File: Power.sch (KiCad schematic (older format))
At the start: 70 parts, among them J3 ESTOP, J4 PWR, J5 Conn_ARM_JTAG_SWD_10, J7 FAN, Q1 MMBT5401LT1G, Q2 PSMN4R8-100BSEJ, Q3 MMBT3904, Q4 Q_NMOS_GDS, Q5 Q_NMOS_GDS, Q6 Q_NMOS_GDS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

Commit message: add part numbers, minor tweaks
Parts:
- C44: footprint Capacitor_SMD:C_0402_1005Metric -> Capacitor_SMD:C_0603_1608Metric; D1PN 311-1039-1-ND -> (none); MFN Yageo -> (none); MPN CC0402KRX7R8BB472 -> (none)
- Q6: value Q_NMOS_GDS -> NTS4001NT1G; footprint Package_TO_SOT_SMD:SOT-416 -> Package_TO_SOT_SMD:SOT-323_SC-70; symbol Device:Q_NMOS_GDS -> Device:Q_NMOS_GSD
- R30: footprint Resistor_SMD:R_0402_1005Metric -> Resistor_SMD:R_0603_1608Metric; D1PN P432KHCT-ND -> (none); MFN Panasonic -> (none); MPN ERJ-3EKF4323V -> (none)
- R31: footprint Resistor_SMD:R_0402_1005Metric -> Resistor_SMD:R_0603_1608Metric
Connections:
- net +12V: now also Q6.3 (D); no longer Q6.2 (D)
- net at Q5.1 (G), R22.1: now also Q6.2 (S); no longer Q6.3 (S)
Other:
- moved on the sheet: C37, Q5, R21
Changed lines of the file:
@@
 Connection ~ 6650 3300
 Connection ~ 6925 1100
-Connection ~ 7000 5050
+Connection ~ 7000 5300
 Connection ~ 7000 5750
 Connection ~ 7000 6000
@@
 	6100 1450 6550 1450
 Wire Wire Line
+	6200 5300 6200 5700
+Wire Wire Line
+	6200 5300 7000 5300
+Wire Wire Line
+	6200 5900 6200 6000
+Wire Wire Line
+	6200 6000 7000 6000
+Wire Wire Line
 	6550 1100 6550 1150
 Wire Wire Line
@@
 	6550 1450 6550 1350
 Wire Wire Line
-	6600 5050 7000 5050
-Wire Wire Line
 	6650 3300 6450 3300
 Wire Wire Line
@@
 	7000 2100 6900 2100
 Wire Wire Line
-	7000 5050 7000 5000
-Wire Wire Line
-	7000 5350 7000 5050
-Wire Wire Line
-	7000 5750 7400 5750
+	7000 5300 7000 5250
+Wire Wire Line
+	7000 5350 7000 5300
+Wire Wire Line
+	7000 5750 7600 5750
 Wire Wire Line
 	7000 5800 7000 5750
 Wire Wire Line
-	7000 6000 7700 6000
+	7000 6000 7900 6000
 Wire Wire Line
 	7000 6050 7000 6000
@@
 	7700 1100 7500 1100
 Wire Wire Line
-	7700 6000 7700 5950
-Wire Wire Line
 	7800 1700 7950 1700
 Wire Wire Line
@@
 Wire Wire Line
 	7800 4250 7800 4050
+Wire Wire Line
+	7900 6000 7900 5950
 Wire Wire Line
 	7950 1900 7800 1900
@@
 Text GLabel 4850 900  2    50   Input ~ 0
 VOUT
-Text GLabel 7700 5350 1    50   Input ~ 0
+Text GLabel 7900 5350 1    50   Input ~ 0
 VOUT
 $Comp
@@
 L power:+12V #PWR0163
 U 1 1 5D69A634
-P 7000 5000
-F 0 "#PWR0163" H 7000 4850 50  0001 C CNN
-F 1 "+12V" H 7015 5173 50  0000 C CNN
-F 2 "" H 7000 5000 50  0001 C CNN
-F 3 "" H 7000 5000 50  0001 C CNN
-	1    7000 5000
+P 7000 5250
+F 0 "#PWR0163" H 7000 5100 50  0001 C CNN
+F 1 "+12V" H 7015 5423 50  0000 C CNN
+F 2 "" H 7000 5250 50  0001 C CNN
+F 3 "" H 7000 5250 50  0001 C CNN
+	1    7000 5250
 	1    0    0    -1
 $EndComp
@@
 F 3 "" H 5450 1450 50  0001 C CNN
 	1    5450 1450
-	-1   0    0    -1
-$EndComp
-$Comp
-L power:GND #PWR0145
-U 1 1 5E52C140
-P 6600 5250
-F 0 "#PWR0145" H 6600 5000 50  0001 C CNN
-F 1 "GND" H 6605 5077 50  0001 C CNN
-F 2 "" H 6600 5250 50  0001 C CNN
-F 3 "" H 6600 5250 50  0001 C CNN
-	1    6600 5250
 	-1   0    0    -1
 $EndComp
@@
 L Device:R_Small R21
 U 1 1 5D281236
-P 7700 5450
-F 0 "R21" H 7759 5496 50  0000 L CNN
-F 1 "10R" H 7759 5405 50  0000 L CNN
-F 2 "Package_TO_SOT_THT:TO-247-2_Vertical" H 7700 5450 50  0001 C CNN
-F 3 "~" H 7700 5450 50  0001 C CNN
-	1    7700 5450
+P 7900 5450
+F 0 "R21" H 7959 5496 50  0000 L CNN
+F 1 "10R" H 7959 5405 50  0000 L CNN
+F 2 "Package_TO_SOT_THT:TO-247-2_Vertical" H 7900 5450 50  0001 C CNN
+F 3 "~" H 7900 5450 50  0001 C CNN
+	1    7900 5450
 	1    0    0    -1
 $EndComp
@@
 F 0 "R30" H 10300 3750 50  0000 L CNN
 F 1 "437k" H 10300 3650 50  0000 L CNN
-F 2 "Resistor_SMD:R_0402_1005Metric" H 10200 3700 60  0001 C CNN
+F 2 "Resistor_SMD:R_0603_1608Metric" H 10200 3700 60  0001 C CNN
 F 3 "~" H 10200 3700 60  0001 C CNN
 F 4 "Digikey" H 10250 3800 50  0001 C CNN "D1N"
-F 5 "P432KHCT-ND" H 10250 3800 50  0001 C CNN "D1PN"
-F 6 "Panasonic" H 10250 3800 50  0001 C CNN "MFN"
-F 7 "ERJ-3EKF4323V" H 10250 3800 50  0001 C CNN "MPN"
+F 5 "" H 10250 3800 50  0001 C CNN "D1PN"
+F 6 "" H 10250 3800 50  0001 C CNN "MFN"
+F 7 "" H 10250 3800 50  0001 C CNN "MPN"
 F 8 "" H 10200 3700 60  0001 C CNN "Maximum Power"
 F 9 "432000" H 10200 3700 60  0001 C CNN "Resistance"
@@
 F 0 "R31" H 10300 4050 50  0000 L CNN
 F 1 "140k" H 10300 3950 50  0000 L CNN
-F 2 "Resistor_SMD:R_0402_1005Metric" H 10200 4000 60  0001 C CNN
+F 2 "Resistor_SMD:R_0603_1608Metric" H 10200 4000 60  0001 C CNN
 F 3 "~" H 10200 4000 60  0001 C CNN
 F 4 "Digikey" H 10250 4100 50  0001 C CNN "D1N"
@@
 $EndComp
 $Comp
+L Device:C_Small C37
+U 1 1 5D7A6A8D
+P 6200 5800
+F 0 "C37" H 6292 5846 50  0000 L CNN
+F 1 "100n" H 6292 5755 50  0000 L CNN
+F 2 "Capacitor_SMD:C_0603_1608Metric" H 6200 5800 50  0001 C CNN
+F 3 "~" H 6200 5800 50  0001 C CNN
+	1    6200 5800
+	1    0    0    -1
+$EndComp
+$Comp
 L Device:C_Small C40
 U 1 1 5D64F8F0
@@
 F 3 "~" H 6550 1250 50  0001 C CNN
 	1    6550 1250
-	1    0    0    -1
-$EndComp
-$Comp
-L Device:C_Small C37
-U 1 1 5D7A6A8D
-P 6600 5150
-F 0 "C37" H 6692 5196 50  0000 L CNN
-F 1 "100n" H 6692 5105 50  0000 L CNN
-F 2 "Capacitor_SMD:C_0603_1608Metric" H 6600 5150 50  0001 C CNN
-F 3 "~" H 6600 5150 50  0001 C CNN
-	1    6600 5150
 	1    0    0    -1
 $EndComp
@@
 F 0 "C44" H 9400 3850 50  0000 L CNN
 F 1 "4n7" H 9400 3950 50  0000 L CNN
-F 2 "Capacitor_SMD:C_0402_1005Metric" H 9300 3950 60  0001 C CNN
+F 2 "Capacitor_SMD:C_0603_1608Metric" H 9300 3950 60  0001 C CNN
 F 3 "~" H 9300 3950 60  0001 C CNN
 F 4 "4n7" H 9300 3950 60  0001 C CNN "Capacitance"
 F 5 "Digikey" H 9400 4000 50  0001 C CNN "D1N"
-F 6 "311-1039-1-ND" H 9400 4000 50  0001 C CNN "D1PN"
-F 7 "Yageo" H 9400 4000 50  0001 C CNN "MFN"
-F 8 "CC0402KRX7R8BB472" H 9400 4000 50  0001 C CNN "MPN"
+F 6 "" H 9400 4000 50  0001 C CNN "D1PN"
+F 7 "" H 9400 4000 50  0001 C CNN "MFN"
+F 8 "" H 9400 4000 50  0001 C CNN "MPN"
 F 9 "25V" H 9400 4050 50  0000 L CNN "Maximum Voltage"
 F 10 "10%" H 9300 3950 60  0001 C CNN "Tolerance"
@@
 $EndComp
 $Comp
-L Device:Q_NMOS_GDS Q6
+L Device:Q_NMOS_GSD Q6
 U 1 1 5D69534E
 P 6900 5550
-F 0 "Q6" H 6950 5750 50  0000 C CNN
-F 1 "Q_NMOS_GDS" V 7152 5550 50  0001 C CNN
-F 2 "Package_TO_SOT_SMD:SOT-416" H 7100 5650 50  0001 C CNN
+F 0 "Q6" H 7150 5700 50  0000 C CNN
+F 1 "NTS4001NT1G" H 7350 5600 50  0000 C CNN
+F 2 "Package_TO_SOT_SMD:SOT-323_SC-70" H 7100 5650 50  0001 C CNN
 F 3 "~" H 6900 5550 50  0001 C CNN
 	1    6900 5550
@@
 L Device:Q_NMOS_GDS Q5
 U 1 1 5D27FC20
-P 7600 5750
-F 0 "Q5" H 7550 5900 50  0000 C CNN
-F 1 "Q_NMOS_GDS" V 7948 5600 50  0001 C CNN
-F 2 "Package_TO_SOT_SMD:TO-263-2" H 7800 5850 50  0001 C CNN
-F 3 "~" H 7600 5750 50  0001 C CNN
-	1    7600 5750
-	1    0    0    -1
-$EndComp
+P 7800 5750
+F 0 "Q5" H 7750 5900 50  0000 C CNN
+F 1 "Q_NMOS_GDS" V 8148 5600 50  0001 C CNN
+F 2 "Package_TO_SOT_SMD:TO-263-2" H 8000 5850 50  0001 C CNN
+F 3 "~" H 7800 5750 50  0001 C CNN
+	1    7800 5750
+	1    0    0    -1
+$EndComp

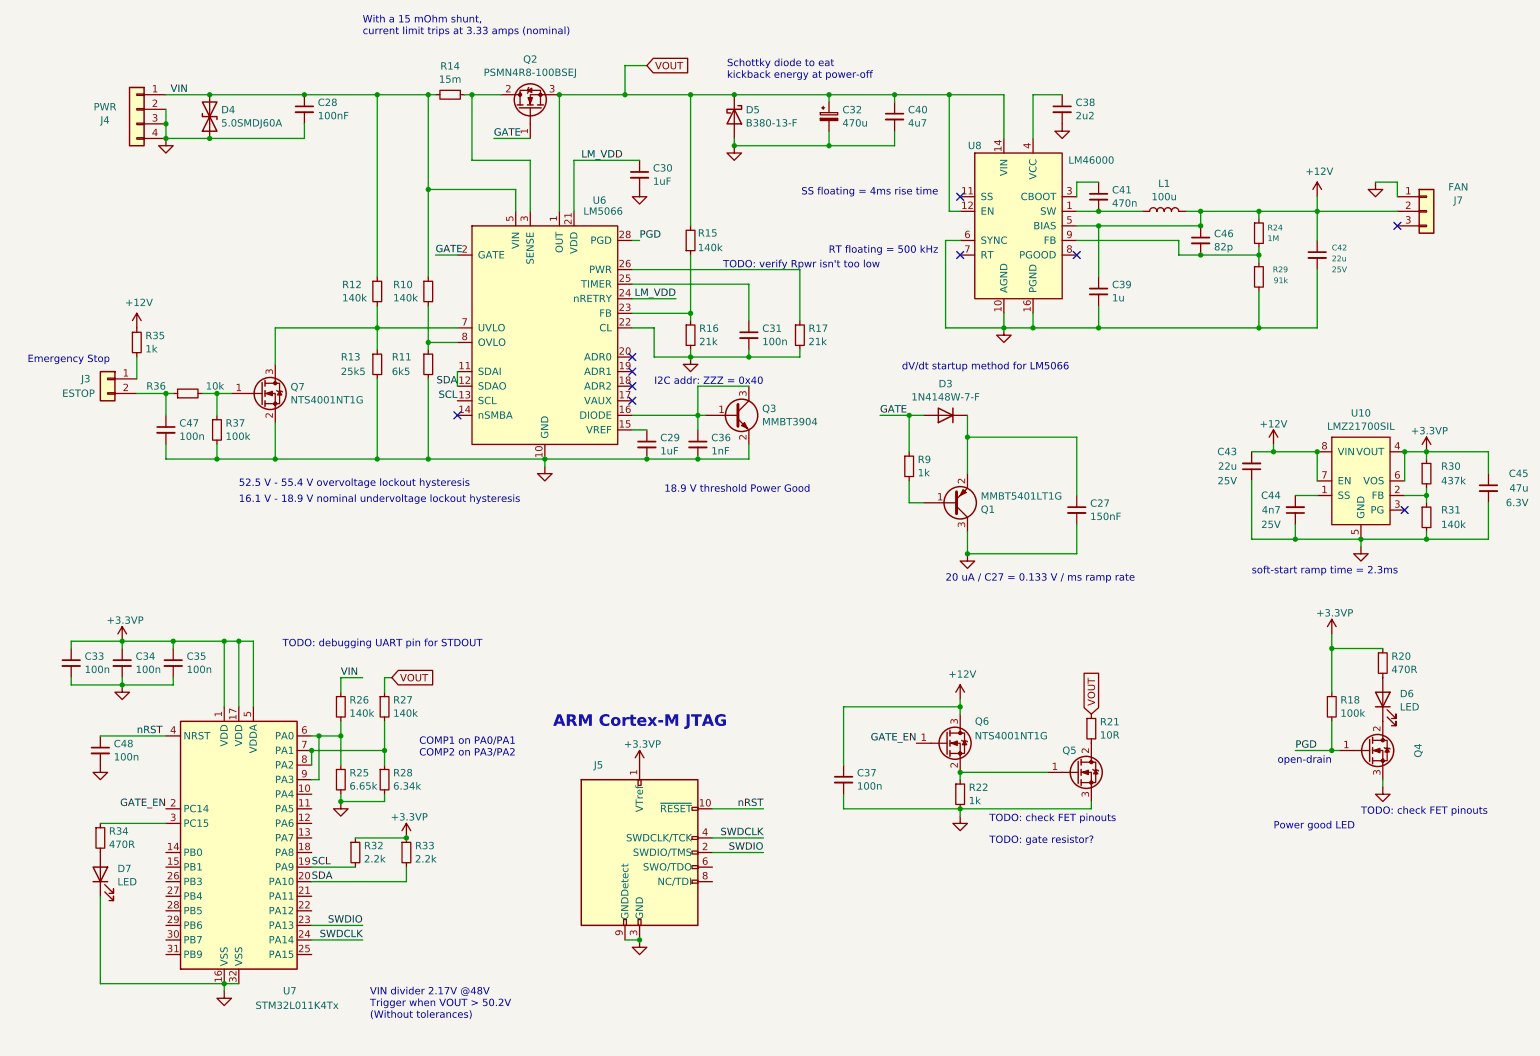
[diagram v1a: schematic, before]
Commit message: add MOSFET drive IC, simply a bit by pushing more into MCU, tweak layout
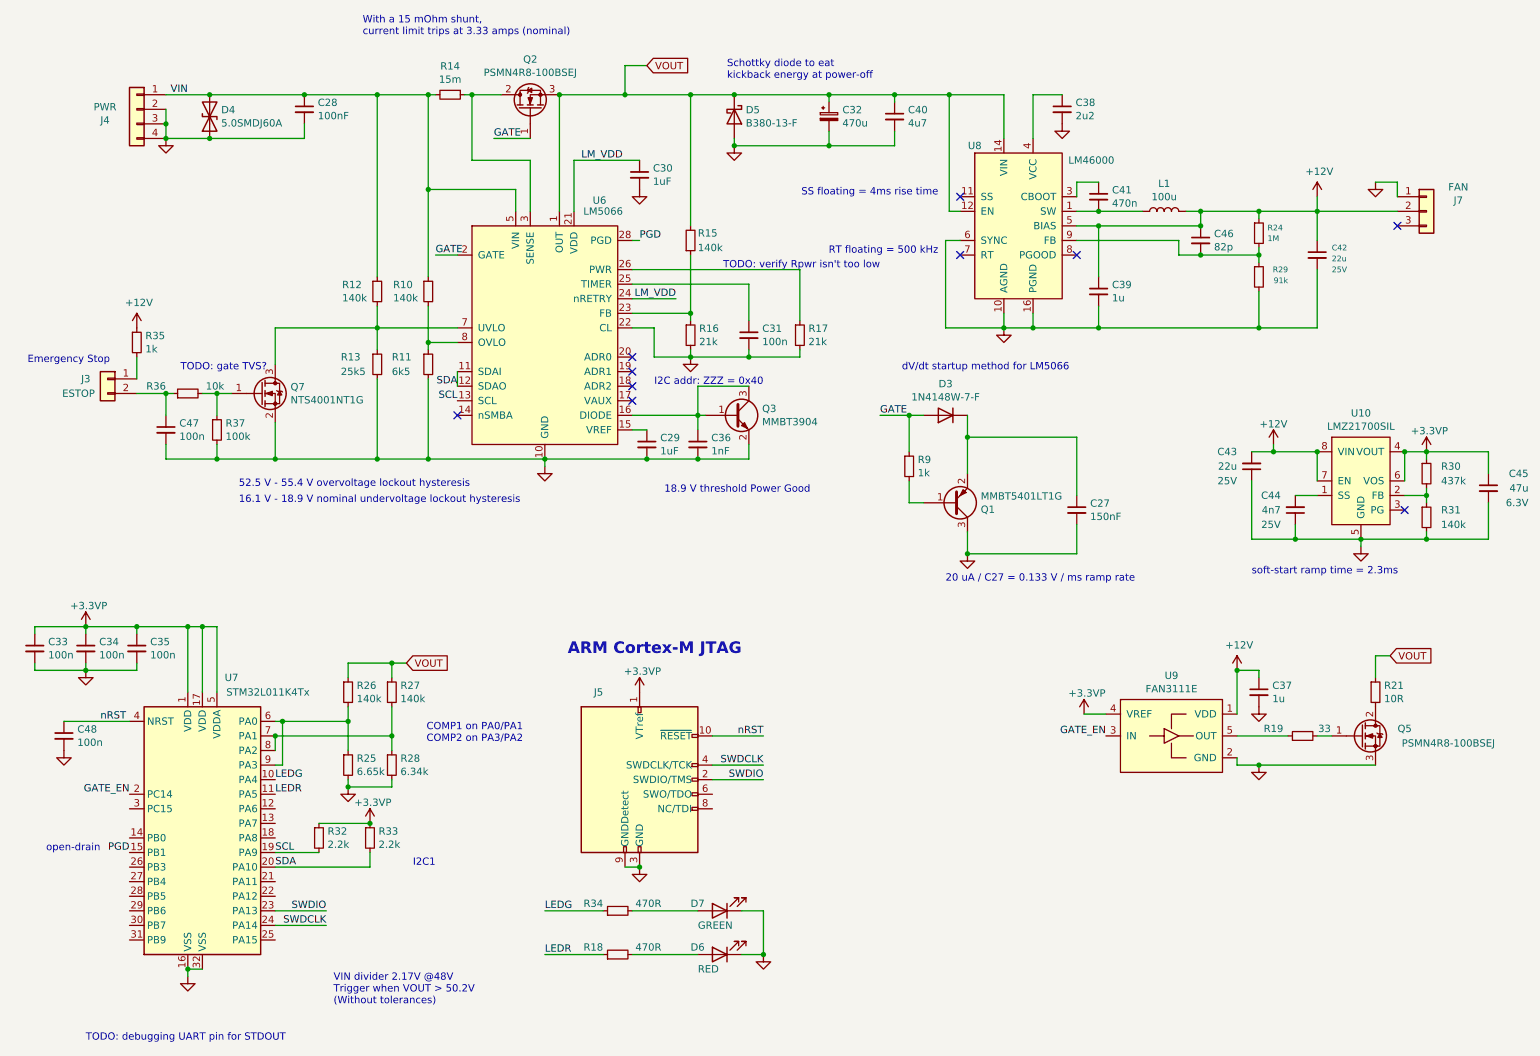
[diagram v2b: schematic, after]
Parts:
- removed Q4: Q_NMOS_GDS, Package_TO_SOT_SMD:SOT-23, symbol Device:Q_NMOS_GDS
- removed Q6: NTS4001NT1G, Package_TO_SOT_SMD:SOT-323_SC-70, symbol Device:Q_NMOS_GSD
- removed R20: 470R, Resistor_SMD:R_0603_1608Metric, symbol Device:R_Small
- removed R22: 1k, Resistor_SMD:R_0603_1608Metric, symbol Device:R_Small
- added R19: 33, Resistor_SMD:R_0603_1608Metric, symbol Device:R_Small
- added U9: FAN3111E, Package_TO_SOT_SMD:SOT-23-5, symbol voltage_translators:FAN3111E
- C37: value 100n -> 1u
- D6: value LED -> RED
- D7: value LED -> GREEN
- Q5: value Q_NMOS_GDS -> PSMN4R8-100BSEJ
- R18: value 100k -> 470R
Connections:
- net +12V: now also U9.1 (VDD)
- net +3.3VP: now also U9.4 (VREF); no longer R18.1
- net GATE_EN: now also U9.3 (IN)
- net GND: now also D6.1 (K), U9.2 (GND)
- net PGD: now also U7.15 (PB1); no longer R18.2
- net VIN: no longer R26.1
- net VOUT: now also R26.1
- net at Q5.1 (G): now also R19.2
- net at D6.2 (A): now also R18.2
- net LEDG: now reaches U7.10 (PA4)
- net LEDG: now also R34.1
- net LEDR: now reaches U7.11 (PA5)
- net LEDR: now also R18.1
- net at U7.3 (PC15): no longer R34.1
- new net: R19.1, U9.5 (OUT)
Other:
- note added: "I2C1"
- note added: "TODO: gate TVS?"
- note removed: "Power good LED"
- note removed: "TODO: check FET pinouts"
- note removed: "TODO: gate resistor?"
- moved on the sheet: C33, C34, C35, C37, C48, D7, J5, Q5, R21, R25, R26, R27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
